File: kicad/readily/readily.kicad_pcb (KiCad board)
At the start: 2 copper layers, 63.5 x 55.9 mm, 33 parts, among them J1 Conn_01x09_Socket, J3 USB_C_Receptacle_USB2.0_16P, SW2 SW_SPST, SW3 SW_SPST, U1 ESP32-S3-WROOM-1, U2 BQ24040DSQR, U3 TPD2EUSB30, U4 TLV75533PDRV, U5 ED08905M-FE15C7_0-C10-2053, U6 WAFER-PH2_0-3PWB

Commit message: feat: updating the screen position
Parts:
- moved J1 20.3 mm to (191.8, 52.0), turned to -90 degrees
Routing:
- net GND: track 278.8 -> 301.1 mm
- net +3V3: track 115.4 -> 136.4 mm, vias 5 -> 6
- net DISP_DISP: track 41.0 -> 50.4 mm
- net DISP_DI: track 33.8 -> 30.4 mm, vias 1 -> 2
- net DISP_CS: track 41.4 -> 43.5 mm, vias 1 -> 2
- net DISP_CLK: track 30.8 -> 30.7 mm, vias 1 -> 2

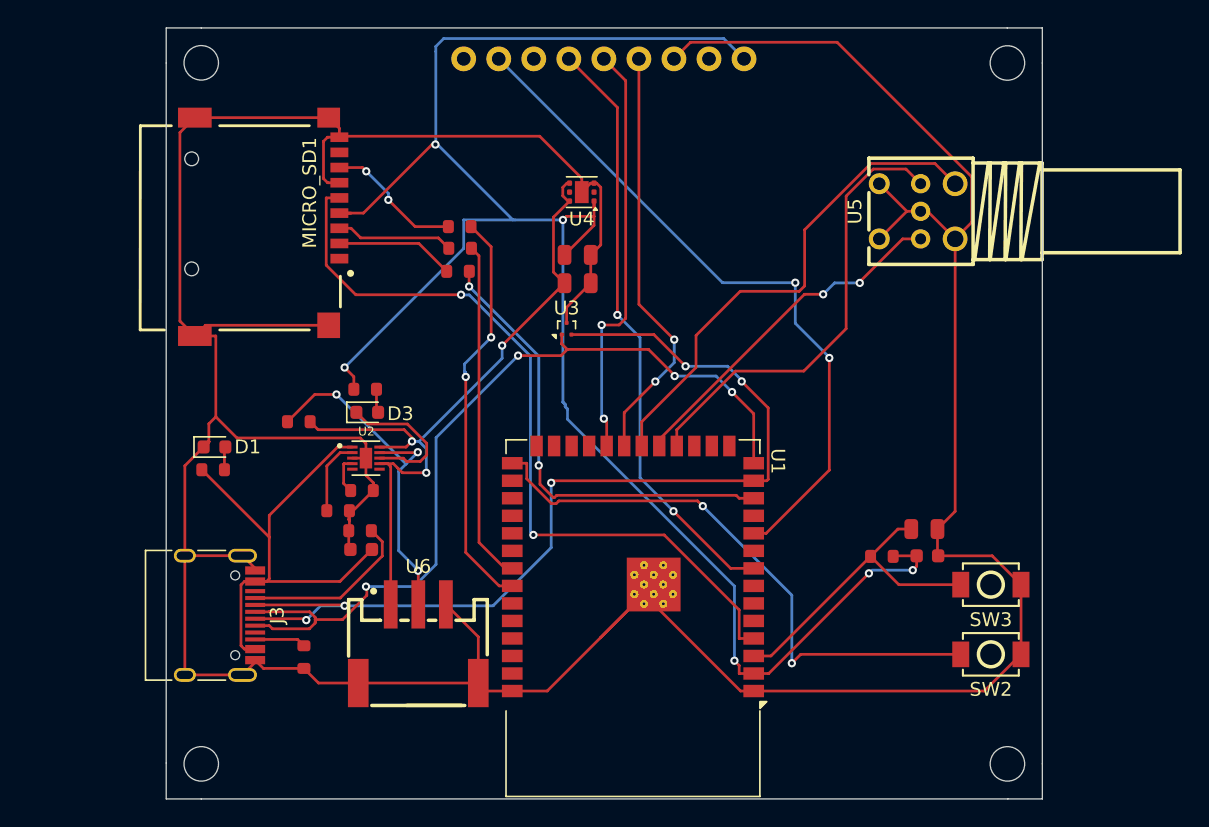
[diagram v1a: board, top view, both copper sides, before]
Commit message: feat: adding logo to pcb, improving component placement and changing the battery connector to two pin JST
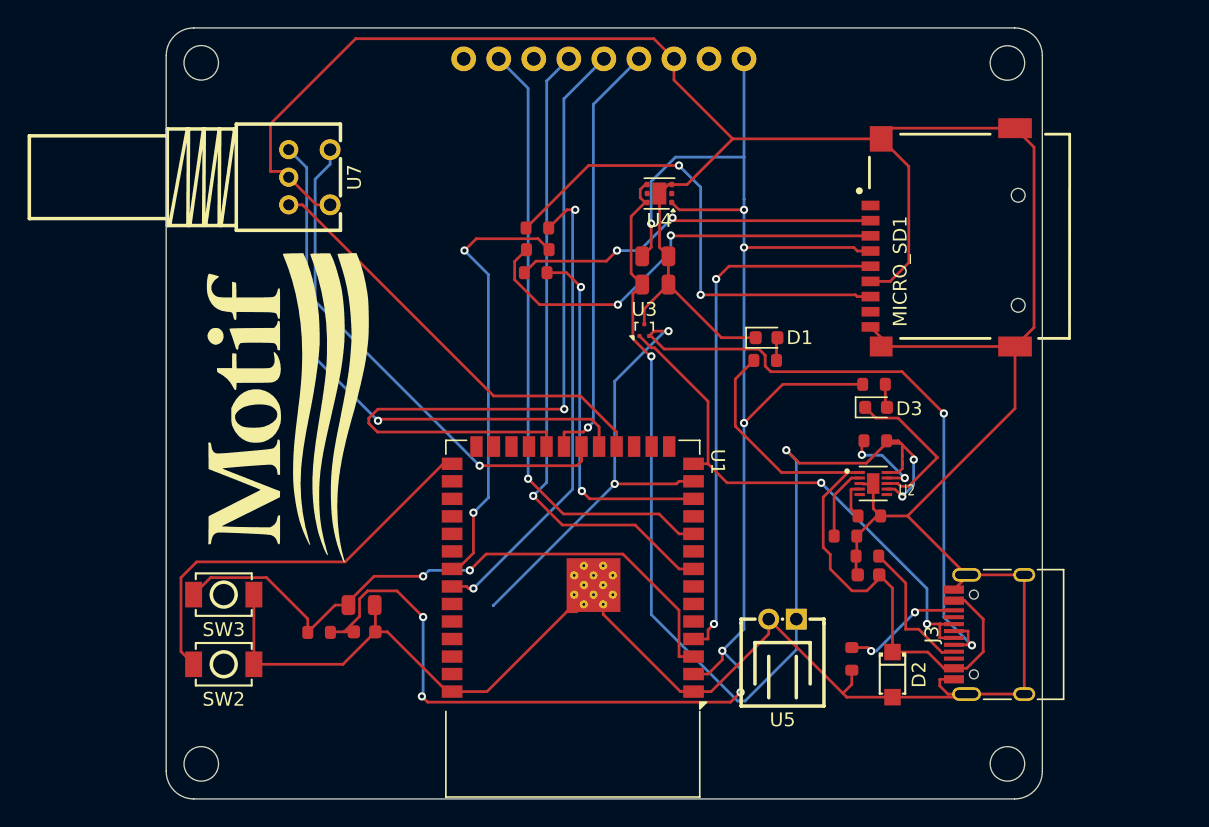
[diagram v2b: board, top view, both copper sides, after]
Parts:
- removed U6: WAFER-PH2_0-3PWB, JLCImport:WAFER-PH2_0-3PWB
- added D2: SMF5_0A_C19077497, JLCImport:SMF5_0A_C19077497, F.Cu at (202.5, 96.6)
- added G***: LOGO, Motiff Icon:motiff_icon, F.Cu at (160.3, 77.0)
- added U7: ED08907M-FB15C7_0-C10-2049, JLCImport:ED08907M-FB15C7_0-C10-2049, F.Cu at (160.3, 60.6)
- U5: value ED08905M-FE15C7_0-C10-2053 -> WAFER-PH2_0-2PWZ; footprint JLCPCB Import:ED08905M-FE15C7_0-C10-2053 -> JLCImport:WAFER-PH2_0-2PWZ
- moved J3 58.8 mm to (211.0, 93.7), turned to 90 degrees
- moved SW2 55.6 mm to (154.1, 95.9)
- moved SW3 55.6 mm to (154.1, 90.8)
- moved MICRO_SD1 52.8 mm to (208.1, 64.9), turned to 90 degrees
- moved R8 41.8 mm to (201.3, 79.7)
- moved R9 41.2 mm to (161.0, 93.6)
- moved C4 41.2 mm to (164.3, 93.5)
- moved C5 41.2 mm to (164.1, 91.6)
- moved D1 40.8 mm to (193.4, 72.2)
- moved R10 40.8 mm to (193.3, 73.9)
- moved R5 39.7 mm to (199.6, 95.5)
- moved D3 36.9 mm to (201.3, 77.3)
- moved R12 36.9 mm to (201.2, 75.6)
- moved C1 36.8 mm to (200.8, 89.4)
- moved R4 36.8 mm to (200.7, 88.0)
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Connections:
- U5 pad 1: RT_SW -> SYS_OUT
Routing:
- net SYS_OUT: track 53.2 -> 82.4 mm, vias 3 -> 4
- net GND: track 301.1 -> 273.4 mm
- net Net-(MICRO_SD1-DAT0): track 10.0 -> 35.3 mm
- net DISP_DI: track 30.4 -> 55.7 mm, vias 2 -> 1
- net EN: track 22.6 -> 46.5 mm, vias 0 -> 2
- net D+: track 62.1 -> 38.7 mm, vias 4 -> 2
- net Net-(MICRO_SD1-CMD): track 8.53 -> 31.9 mm, vias 0 -> 2
- net BAT_NTC: track 26.6 -> 6.23 mm, vias 3 -> 2
- net Net-(MICRO_SD1-CD/DAT3): track 8.62 -> 26.8 mm, vias 0 -> 2
- net SD_CLK: track 56.7 -> 39.0 mm
- net RT_DT: track 25.4 -> 40.1 mm, vias 2 -> 1
- net GPIO0: track 44.2 -> 29.7 mm, vias 2 -> 0
- net +5V: track 36.8 -> 47.1 mm
- net SD_CS: track 34.1 -> 26.1 mm
- net +3V3: track 136.4 -> 128.4 mm, vias 6 -> 8
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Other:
- outline, holes or cut-outs redrawn

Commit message: feat: adding a GND plane to achieve higher power stability and heat management
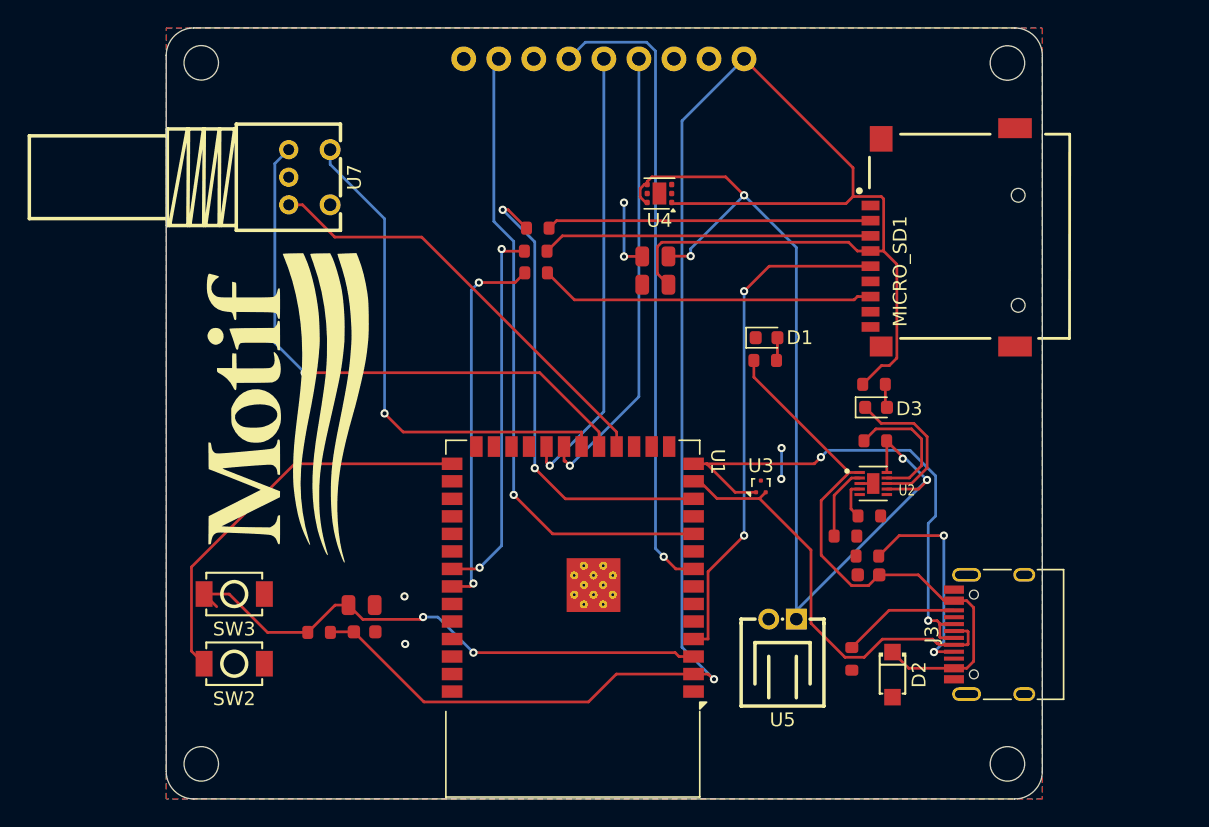
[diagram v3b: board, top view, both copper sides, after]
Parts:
- moved U3 14.1 mm to (193.0, 83.0)
- moved R13 3.25 mm to (176.7, 67.5), turned to 0 degrees
- moved R11 3.23 mm to (176.8, 64.3), turned to 0 degrees
- moved C3 2.06 mm to (185.3, 68.4), turned to 180 degrees
- moved C2 2.04 mm to (185.3, 66.3), turned to 180 degrees
- moved SW2 0.76 mm to (154.8, 95.8)
- moved SW3 0.76 mm to (154.8, 90.8)
- moved R14 0.19 mm to (176.7, 65.9), turned to 0 degrees
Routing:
- net GND: track 273.4 -> 8.47 mm, vias 0 -> 6
- net D-: track 78.0 -> 31.6 mm, vias 4 -> 0
- net DISP_DI: track 55.7 -> 32.6 mm
- net +3V3: track 128.4 -> 142.7 mm, vias 8 -> 1
- net Net-(MICRO_SD1-DAT0): track 35.3 -> 24.3 mm, vias 2 -> 0
- net SYS_OUT: track 82.4 -> 73.2 mm
- net SD_CS: track 26.1 -> 34.4 mm
- net Net-(MICRO_SD1-CMD): track 31.9 -> 23.9 mm, vias 2 -> 0
- net SD_MISO: track 34.6 -> 27.4 mm
- net EN: track 46.5 -> 40.4 mm
- net Net-(J3-CC1): track 9.69 -> 15.5 mm, vias 0 -> 2
- net +5V: track 47.1 -> 42.3 mm
- net SD_MOSI: track 31.9 -> 27.5 mm
- net BAT_NTC: track 6.23 -> 9.66 mm, vias 2 -> 0
- net Net-(MICRO_SD1-CD/DAT3): track 26.8 -> 23.5 mm, vias 2 -> 0
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- added copper zone on B.Cu, net GND
- added copper zone on F.Cu, net GND

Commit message: feat: finishing the power refactor on the board
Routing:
- net +3V3: track 142.7 -> 148.3 mm

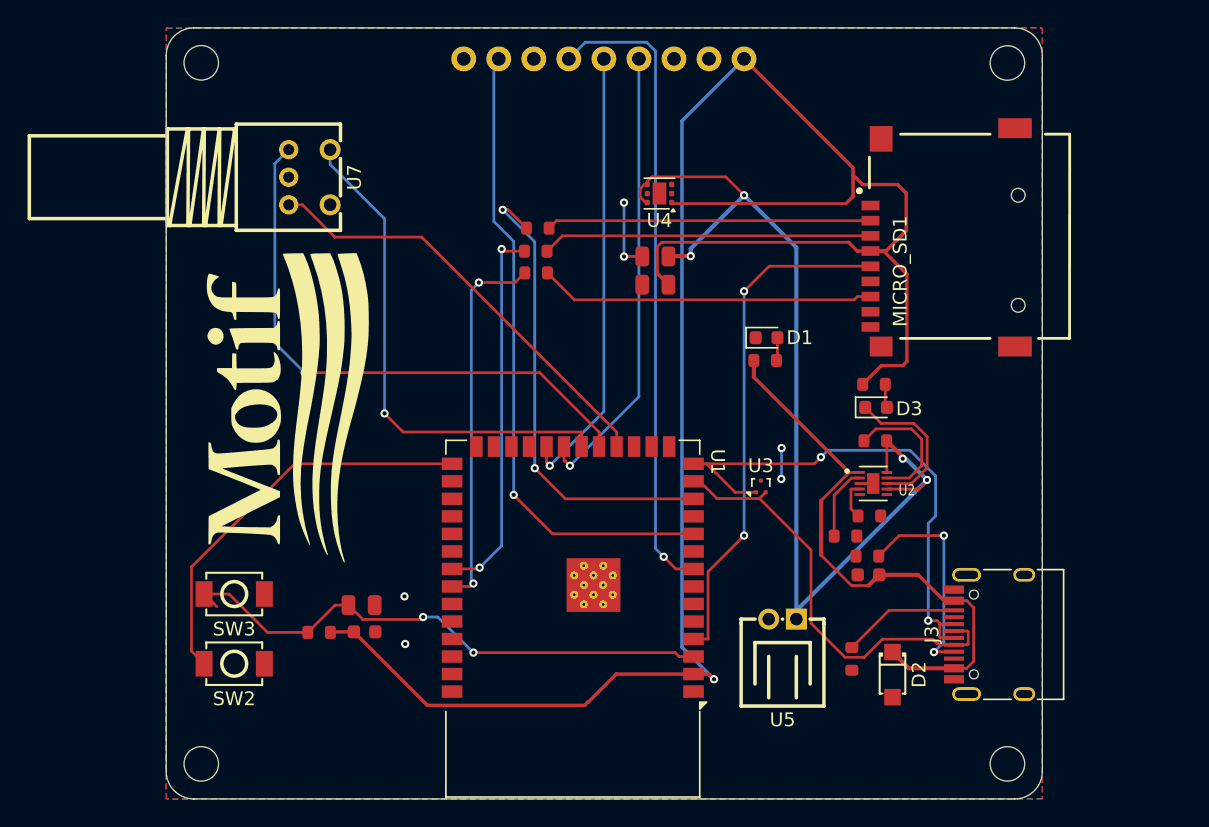
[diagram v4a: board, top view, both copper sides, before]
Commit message: feat: updating and rerouting all components
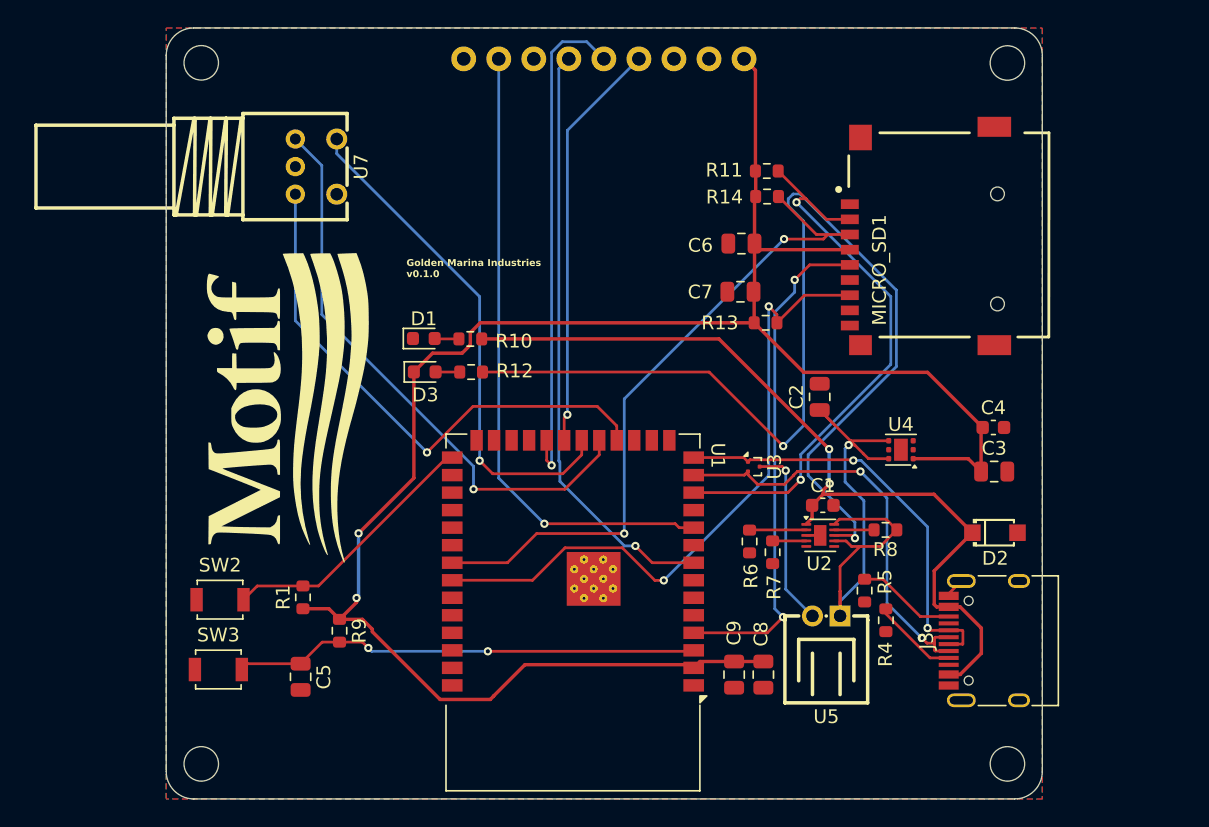
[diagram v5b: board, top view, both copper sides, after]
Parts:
- added C6: 47uF, Capacitor_SMD:C_0805_2012Metric, F.Cu at (191.6, 65.4)
- added C7: 100nF, Capacitor_SMD:C_0805_2012Metric, F.Cu at (191.5, 68.9)
- added C8: 100nF, Capacitor_SMD:C_0805_2012Metric, F.Cu at (193.2, 96.6)
- added C9: 10uF, Capacitor_SMD:C_0805_2012Metric, F.Cu at (191.1, 96.6)
- added R1: 10K, Resistor_SMD:R_0603_1608Metric, F.Cu at (159.8, 91.0)
- C1: value 4.7uF 0603 -> 4.7uF; footprint PCM_JLCPCB:C_0603 -> Capacitor_SMD:C_0603_1608Metric
- C2: value 10uF 0805 -> 22uF; footprint PCM_JLCPCB:C_0805 -> Capacitor_SMD:C_0805_2012Metric
- C3, C5: value 10uF 0805 -> 10uF; footprint PCM_JLCPCB:C_0805 -> Capacitor_SMD:C_0805_2012Metric
- C4: value 100nF 0603 -> 100n; footprint PCM_JLCPCB:C_0603 -> Capacitor_SMD:C_0603_1608Metric
- D1: value White 0603 -> LED
- D3: value LED 0603 -> LED
- MICRO_SD1: footprint TF-01A:TF-01A -> SD_Card:TF-01A
- R10, R9: value 5.1KΩ 0603 -> 5.1K; footprint PCM_JLCPCB:R_0603 -> Resistor_SMD:R_0603_1608Metric
- R11, R13, R14, R8: value 10kΩ 0603 -> 10kΩ; footprint PCM_JLCPCB:R_0603 -> Resistor_SMD:R_0603_1608Metric
- R12: value 2.2KΩ 0603 -> 2.2K; footprint PCM_JLCPCB:R_0603 -> Resistor_SMD:R_0603_1608Metric
- R4, R5: value 5.1kΩ 0603 -> 5.1kΩ; footprint PCM_JLCPCB:R_0603 -> Resistor_SMD:R_0603_1608Metric
- R6: value 1kΩ 0603 -> 1kΩ; footprint PCM_JLCPCB:R_0603 -> Resistor_SMD:R_0603_1608Metric
- R7: value 10kΩ 0603 -> 2kΩ; footprint PCM_JLCPCB:R_0603 -> Resistor_SMD:R_0603_1608Metric
- SW2, SW3: footprint JLCImport:TS-1088-AR02016 -> Button_Switch_SMD:SW_SPST_B3U-1000P
- U2: footprint BQ24040DSQR:SON40P200X200X80-11N -> Package_DFN_QFN:Texas_DSQ0010A_WSON-10-1EP_2x2mm_P0.4mm_EP0.9x1.5mm
- moved C4 47.9 mm to (209.8, 78.7)
- moved D3 32.8 mm to (168.6, 74.7)
- moved R12 29.2 mm to (172.0, 74.7), turned to 180 degrees
- moved C3 28.0 mm to (209.9, 81.9), turned to 0 degrees
- moved U4 25.5 mm to (203.2, 80.3)
- moved D1 24.8 mm to (168.6, 72.3)
- moved R10 21.4 mm to (171.9, 72.3), turned to 180 degrees
- moved R14 17.2 mm to (193.4, 62.0), turned to 180 degrees
- moved R11 17.1 mm to (193.4, 60.1), turned to 180 degrees
- moved R13 17.0 mm to (193.3, 71.1), turned to 180 degrees
- moved C2 15.7 mm to (197.3, 76.5), turned to 90 degrees
- moved D2 12.7 mm to (210.0, 86.3), turned to 0 degrees
- moved R7 7.49 mm to (193.8, 87.8), turned to 90 degrees
- moved R6 6.96 mm to (192.2, 87.0), turned to 90 degrees
- moved C5 6.82 mm to (159.6, 96.8), turned to -90 degrees
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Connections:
- net BAT_NTC renamed Net-(U2-TS)
- D3 pad 1: BAT_CHG -> +3V3
- MICRO_SD1 pad 2: Net-(MICRO_SD1-CD/DAT3) -> SD_CS
- MICRO_SD1 pad 3: Net-(MICRO_SD1-CMD) -> SD_MOSI
- MICRO_SD1 pad 7: Net-(MICRO_SD1-DAT0) -> SD_MISO
- R11 pad 2: Net-(MICRO_SD1-CD/DAT3) -> +3V3
- R12 pad 1: +3V3 -> BAT_CHG
- R13 pad 2: Net-(MICRO_SD1-DAT0) -> +3V3
- R14 pad 2: Net-(MICRO_SD1-CMD) -> +3V3
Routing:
- net BAT_CHG: track 11.0 -> 77.5 mm, vias 0 -> 2
- net SYS_OUT: track 73.2 -> 42.7 mm, vias 4 -> 1
- net Net-(MICRO_SD1-DAT0): track 24.3 -> 0.00 mm
- net Net-(MICRO_SD1-CMD): track 23.9 -> 0.00 mm
- net Net-(MICRO_SD1-CD/DAT3): track 23.5 -> 0.00 mm
- net SD_MOSI: track 27.5 -> 49.1 mm
- net SD_MISO: track 27.4 -> 47.8 mm
- net +5V: track 42.3 -> 61.9 mm, vias 0 -> 2
- net GPIO0: track 29.4 -> 19.4 mm
- net Net-(J3-CC1): track 15.5 -> 6.24 mm, vias 2 -> 0
- net +3V3: track 148.3 -> 139.5 mm, vias 1 -> 2
- net RT_CLK: track 31.6 -> 39.4 mm, vias 0 -> 1
- net GND: track 8.47 -> 15.8 mm, vias 6 -> 1
- net SD_CS: track 34.4 -> 41.2 mm
- net Net-(U2-TS): track 9.66 -> 2.89 mm
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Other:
- board text added: "Golden Marina Industries v0.1.0"

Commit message: feat: switching the battery JST and generating the final files for next print
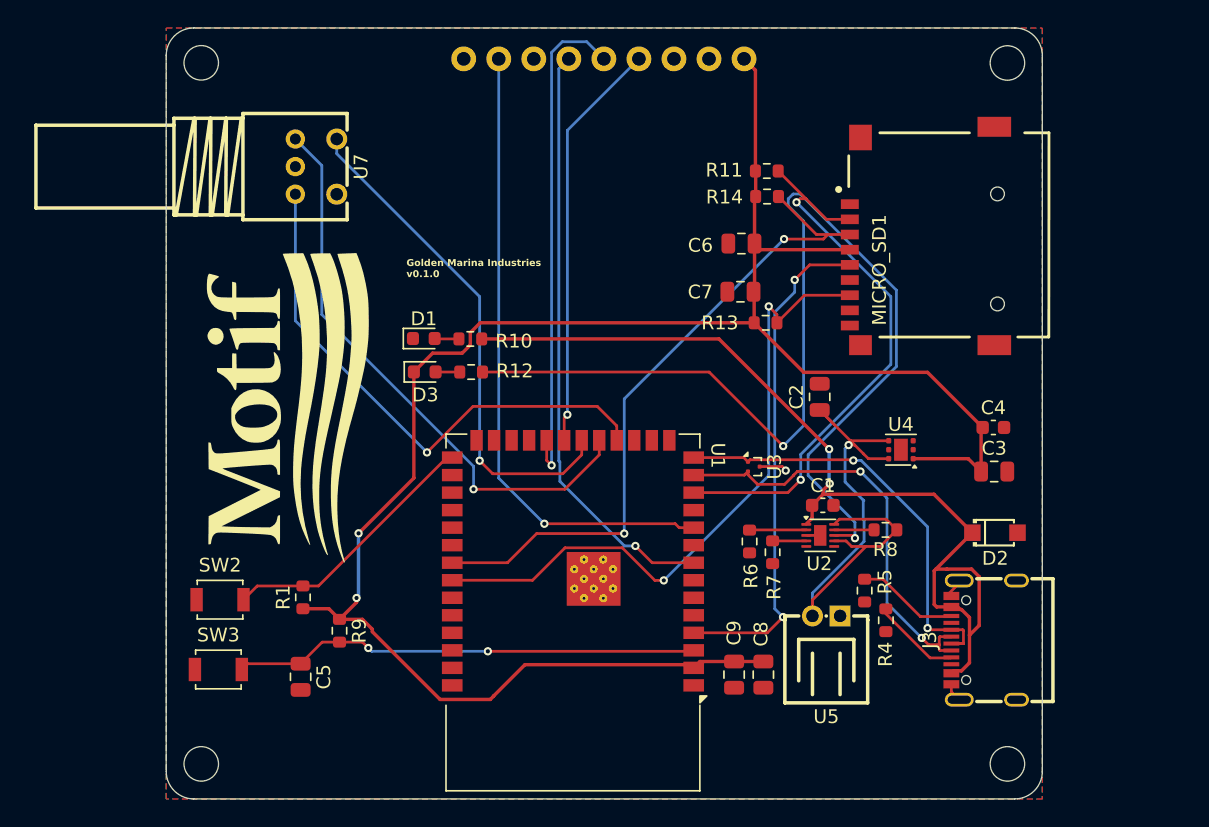
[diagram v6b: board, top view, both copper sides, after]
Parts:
- C4: value 100n -> 100nF
- D1: value LED -> White LED
- D3: value LED -> LED White
- J3: footprint Connector_USB:USB_C_Receptacle_HRO_TYPE-C-31-M-12 -> JLCImport:TYPE-C16PIN
- moved J3 1.49 mm to (209.2, 94.1)
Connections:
- U5 pad 1: SYS_OUT -> GND
- U5 pad 2: GND -> SYS_OUT
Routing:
- net GND: track 15.8 -> 5.83 mm
- net +5V: track 61.9 -> 68.5 mm
- net D+: track 31.1 -> 32.3 mm
